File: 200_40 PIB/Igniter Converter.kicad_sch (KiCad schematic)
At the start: 57 parts, among them Q1 EPC2302, T1 Arthur, U1 LM5022MM, U2 TLVH431BQDCKT, U3 LTV-817-C

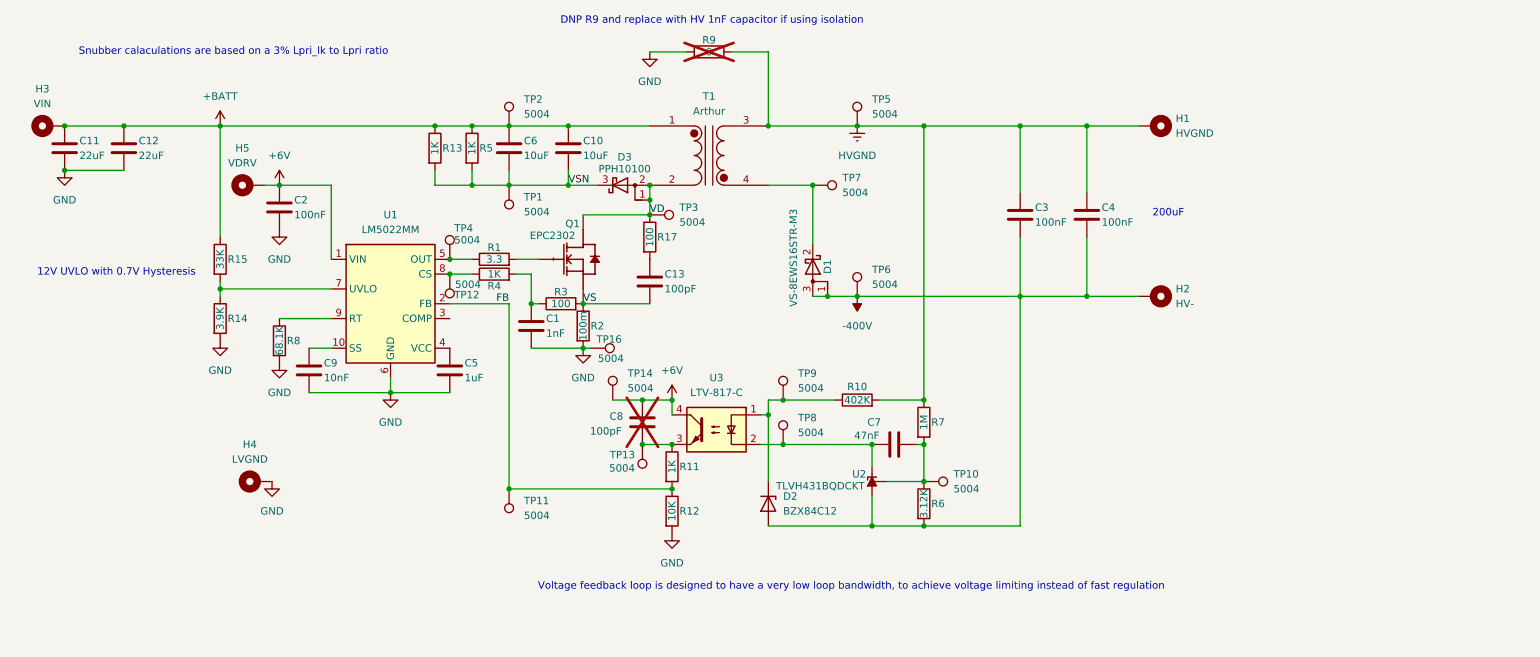
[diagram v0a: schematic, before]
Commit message: Summer 2026 Updates
Created symbol, footprint, and 3D model libraries. Redesigned PIB.
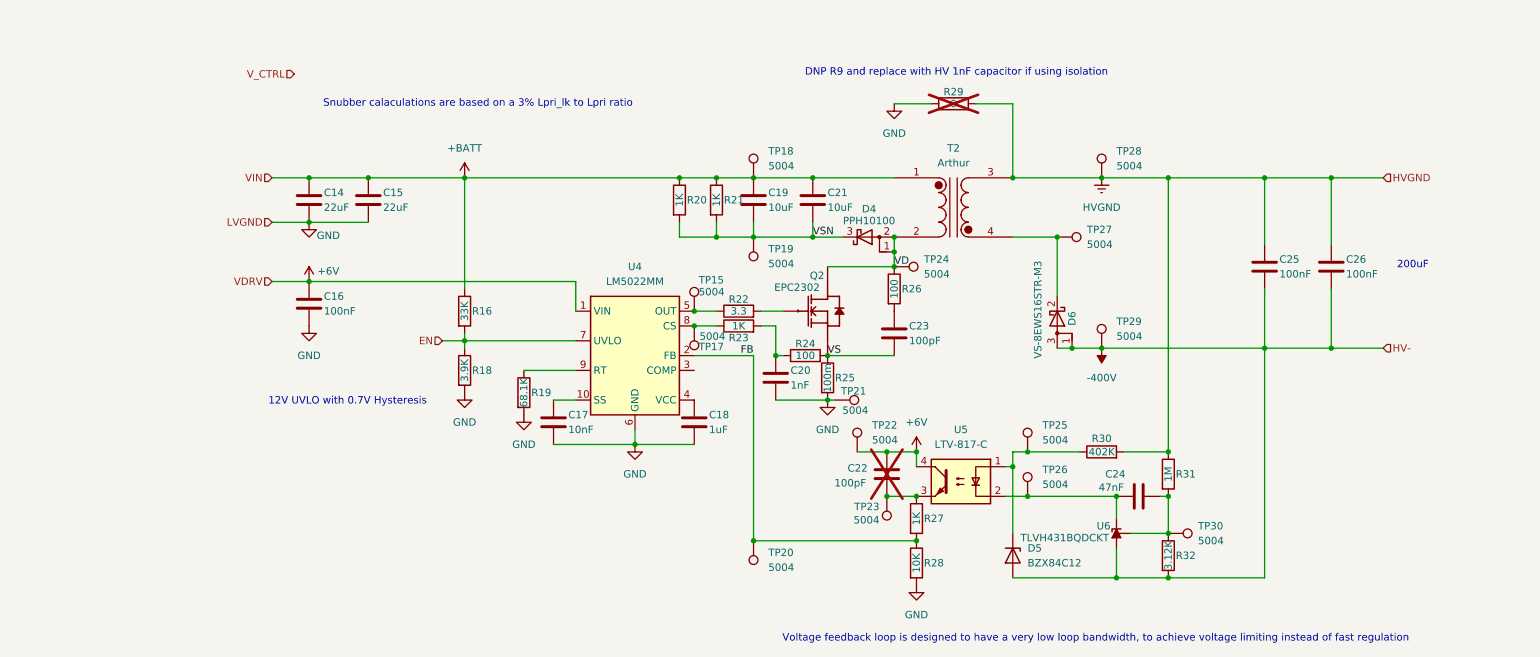
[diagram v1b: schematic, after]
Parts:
- removed C1: 1nF, Capacitor_SMD:C_0402_1005Metric, symbol Device:C
- removed C10, C6: 10uF, Capacitor_SMD:C_1210_3225Metric, symbol Device:C
- removed C11, C12: 22uF, Capacitor_SMD:C_1210_3225Metric, symbol Device:C
- removed C13, C8: 100pF, Capacitor_SMD:C_0603_1608Metric, symbol Device:C
- removed C2: 100nF, Capacitor_SMD:C_0402_1005Metric, symbol Device:C
- removed C3, C4: 100nF, Capacitor_SMD:C_2220_5750Metric, symbol Device:C
- removed C5: 1uF, Capacitor_SMD:C_0402_1005Metric, symbol Device:C
- removed C7: 47nF, Capacitor_SMD:C_0603_1608Metric, symbol Device:C
- removed C9: 10nF, Capacitor_SMD:C_0402_1005Metric, symbol Device:C
- removed D1: VS-8EWS16STR-M3, Package_TO_SOT_SMD:TO-252-2, symbol Device:D_Schottky_AKA
- removed D2: BZX84C12, Package_TO_SOT_SMD:SOT-23, symbol Diode:BZX84Cxx
- removed D3: PPH10100, Package_TO_SOT_SMD:TO-277A, symbol Device:D_Schottky_AAK
- removed H1: HVGND, Pads_Custom:Pad6x4, symbol Mechanical:MountingHole_Pad
- removed H2: HV-, Pads_Custom:Pad6x4, symbol Mechanical:MountingHole_Pad
- removed H3: VIN, Pads_Custom:Pad6x4, symbol Mechanical:MountingHole_Pad
- removed H4: LVGND, Pads_Custom:Pad6x4, symbol Mechanical:MountingHole_Pad
- removed H5: VDRV, Pads_Custom:Pad6x4, symbol Mechanical:MountingHole_Pad
- removed Q1: EPC2302, EPC_FETs:D0606F_100V, symbol EPC_FETs:EPC2302
- removed R1: 3.3, Resistor_SMD:R_0402_1005Metric, symbol Device:R
- removed R10: 402K, Resistor_SMD:R_2512_6332Metric, symbol Device:R
- removed R11: 1K, Resistor_SMD:R_0603_1608Metric, symbol Device:R
- removed R12: 10K, Resistor_SMD:R_0603_1608Metric, symbol Device:R
- removed R13, R5: 1K, Resistor_SMD:R_0805_2012Metric, symbol Device:R
- removed R14: 3.9K, Resistor_SMD:R_0603_1608Metric, symbol Device:R
- removed R15: 33K, Resistor_SMD:R_0603_1608Metric, symbol Device:R
- removed R17: 100, Resistor_SMD:R_0603_1608Metric, symbol Device:R
- removed R2: 100m, Resistor_SMD:R_1225_3264Metric, symbol Device:R
- removed R3: 100, Resistor_SMD:R_0402_1005Metric, symbol Device:R
- removed R4: 1K, Resistor_SMD:R_0402_1005Metric, symbol Device:R
- removed R6: 3.12K, Resistor_SMD:R_0603_1608Metric, symbol Device:R
- removed R7: 1M, Resistor_SMD:R_2512_6332Metric, symbol Device:R
- removed R8: 68.1K, Resistor_SMD:R_0402_1005Metric, symbol Device:R
- removed R9: 0, Resistor_SMD:R_2010_5025Metric, symbol Device:R
- removed T1: Arthur, PlanarTransformer:40-2Transformer, symbol transformer:Transformer_1P_1S_Dot
- removed TP1, TP10, TP11, TP12, TP13, TP14, TP16, TP2, TP3, TP4, TP5, TP6, TP7, TP8, TP9: 5004, TestPoint:TestPoint_Keystone_5000-5004_Miniature, symbol Connector:TestPoint
- removed U1: LM5022MM, Package_SO:MSOP-10_3x3mm_P0.5mm, symbol Regulator_Switching:LM5022MM
- removed U2: TLVH431BQDCKT, Package_TO_SOT_SMD:SOT-363_SC-70-6, symbol Reference_Voltage:TL431DCK
- removed U3: LTV-817-C, Package_DIP:DIP-4_W7.62mm, symbol Isolator:LTV-817
- added C14, C15: 22uF, Capacitor_SMD:C_1210_3225Metric, symbol Device:C
- added C16: 100nF, Capacitor_SMD:C_0402_1005Metric, symbol Device:C
- added C17: 10nF, Capacitor_SMD:C_0402_1005Metric, symbol Device:C
- added C18: 1uF, Capacitor_SMD:C_0402_1005Metric, symbol Device:C
- added C19, C21: 10uF, Capacitor_SMD:C_1210_3225Metric, symbol Device:C
- added C20: 1nF, Capacitor_SMD:C_0402_1005Metric, symbol Device:C
- added C22, C23: 100pF, Capacitor_SMD:C_0603_1608Metric, symbol Device:C
- added C24: 47nF, Capacitor_SMD:C_0603_1608Metric, symbol Device:C
- added C25, C26: 100nF, Capacitor_SMD:C_2220_5750Metric, symbol Device:C
- added D4: PPH10100, Package_TO_SOT_SMD:TO-277A, symbol Device:D_Schottky_AAK
- added D5: BZX84C12, Package_TO_SOT_SMD:SOT-23, symbol Diode:BZX84Cxx
- added D6: VS-8EWS16STR-M3, Package_TO_SOT_SMD:TO-252-2, symbol Device:D_Schottky_AKA
- added Q2: EPC2302, EPC_FETs:D0606F_100V, symbol EPC_FETs:EPC2302
- added R16: 33K, Resistor_SMD:R_0603_1608Metric, symbol Device:R
- added R18: 3.9K, Resistor_SMD:R_0603_1608Metric, symbol Device:R
- added R19: 68.1K, Resistor_SMD:R_0402_1005Metric, symbol Device:R
- added R20, R21: 1K, Resistor_SMD:R_0805_2012Metric, symbol Device:R
- added R22: 3.3, Resistor_SMD:R_0402_1005Metric, symbol Device:R
- added R23: 1K, Resistor_SMD:R_0402_1005Metric, symbol Device:R
- added R24: 100, Resistor_SMD:R_0402_1005Metric, symbol Device:R
- added R25: 100m, Resistor_SMD:R_1225_3264Metric, symbol Device:R
- added R26: 100, Resistor_SMD:R_0603_1608Metric, symbol Device:R
- added R27: 1K, Resistor_SMD:R_0603_1608Metric, symbol Device:R
- added R28: 10K, Resistor_SMD:R_0603_1608Metric, symbol Device:R
- added R29: 0, Resistor_SMD:R_2010_5025Metric, symbol Device:R
- added R30: 402K, Resistor_SMD:R_2512_6332Metric, symbol Device:R
- added R31: 1M, Resistor_SMD:R_2512_6332Metric, symbol Device:R
- added R32: 3.12K, Resistor_SMD:R_0603_1608Metric, symbol Device:R
- added T2: Arthur, PlanarTransformer:40-2Transformer, symbol transformer:Transformer_1P_1S_Dot
- added TP15, TP17, TP18, TP19, TP20, TP21, TP22, TP23, TP24, TP25, TP26, TP27, TP28, TP29, TP30: 5004, TestPoint:TestPoint_Keystone_5000-5004_Miniature, symbol Connector:TestPoint
- added U4: LM5022MM, Package_SO:MSOP-10_3x3mm_P0.5mm, symbol Regulator_Switching:LM5022MM
- added U5: LTV-817-C, Package_DIP:DIP-4_W7.62mm, symbol Isolator:LTV-817
- added U6: TLVH431BQDCKT, Package_TO_SOT_SMD:SOT-363_SC-70-6, symbol Reference_Voltage:TL431DCK
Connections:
- net +6V: now also C16.1, C22.2, TP22.1, U4.1 (VIN), U5.4
- net +BATT: now also C14.1, C15.1, C19.1, C21.1, R16.1, R20.1, R21.1, T2.1 (AA), TP18.1
- net -400V: now also C25.2, C26.2, D5.1 (A), D6.1 (A), D6.3 (A), R32.2, TP29.1, U6.6 (A)
- net FB: now also R27.2, R28.1, TP20.1, U4.2 (FB)
- net GND: now also C14.2, C15.2, C16.2, C17.2, C18.2, C20.2, R18.2, R19.2, R25.2, R28.2, R29.1, TP21.1, U4.6 (GND)
- net HVGND: now also C25.1, C26.1, R29.2, R30.2, R31.1, T2.3 (SA), TP28.1
- net VD: now also D4.1 (A), D4.2 (A), Q2.3 (D), Q2.5 (D), Q2.7 (D), R26.1, T2.2 (AB), TP24.1
- net VS: now also C23.2, Q2.2 (S), Q2.4 (S), Q2.6 (S), R24.2, R25.1
- net VSN: now also C19.2, C21.2, D4.3 (K), R20.2, R21.2, TP19.1
- new net: C24.2, R31.2, R32.1, TP30.1, U6.3 (REF)
- new net: R22.1, TP15.1, U4.5 (OUT)
- new net: C22.1, R27.1, TP23.1, U5.3
- new net: R19.1, U4.9 (RT)
- new net: C18.1, U4.4 (VCC)
- new net: Q2.1 (G), R22.2
- new net: C20.1, R23.2, R24.1
- new net: D6.2 (K), T2.4 (SB), TP27.1
- new net: C24.1, TP26.1, U5.2, U6.1 (K)
- new net: C23.1, R26.2
- new net: C17.1, U4.10 (SS)
- new net: R23.1, TP17.1, U4.8 (CS)
- new net: D5.3 (K), R30.1, TP25.1, U5.1
- new net EN: R16.2, R18.1, U4.7 (UVLO)

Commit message: pretty pib that doesnt work
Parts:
- removed TP15, TP17, TP18, TP19, TP20, TP21, TP22, TP23, TP24, TP25, TP26, TP27, TP28, TP29, TP30: 5004, TestPoint:TestPoint_Keystone_5000-5004_Miniature, symbol Connector:TestPoint
